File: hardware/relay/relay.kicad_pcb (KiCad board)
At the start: 2 copper layers, 65.5 x 22 mm, 18 parts, among them J1 GS3, J2 GS3, J3 CONN_02X04, J4 CONN_01X04, Q1 BC817-40, Q2 BC817-40, U1 ATTINY85-20SU, U2 ATTINY85-20PU

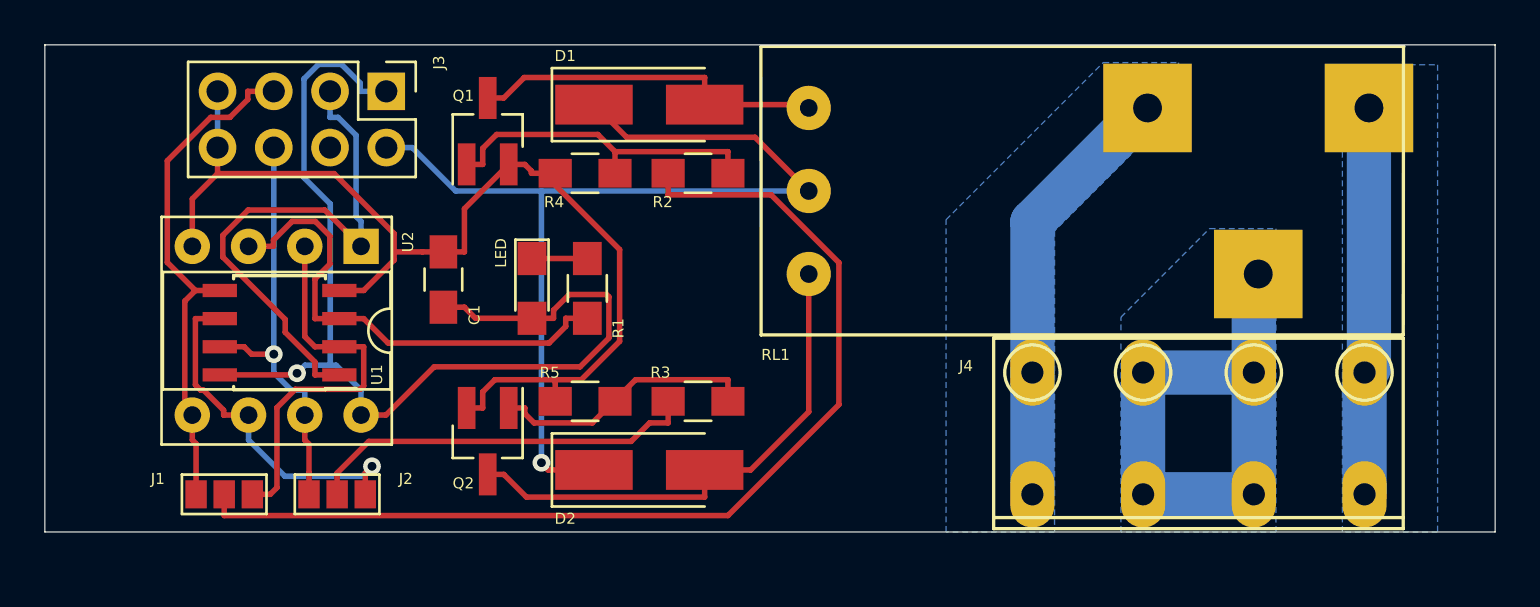
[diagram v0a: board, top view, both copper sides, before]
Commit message: Fix relay footprint
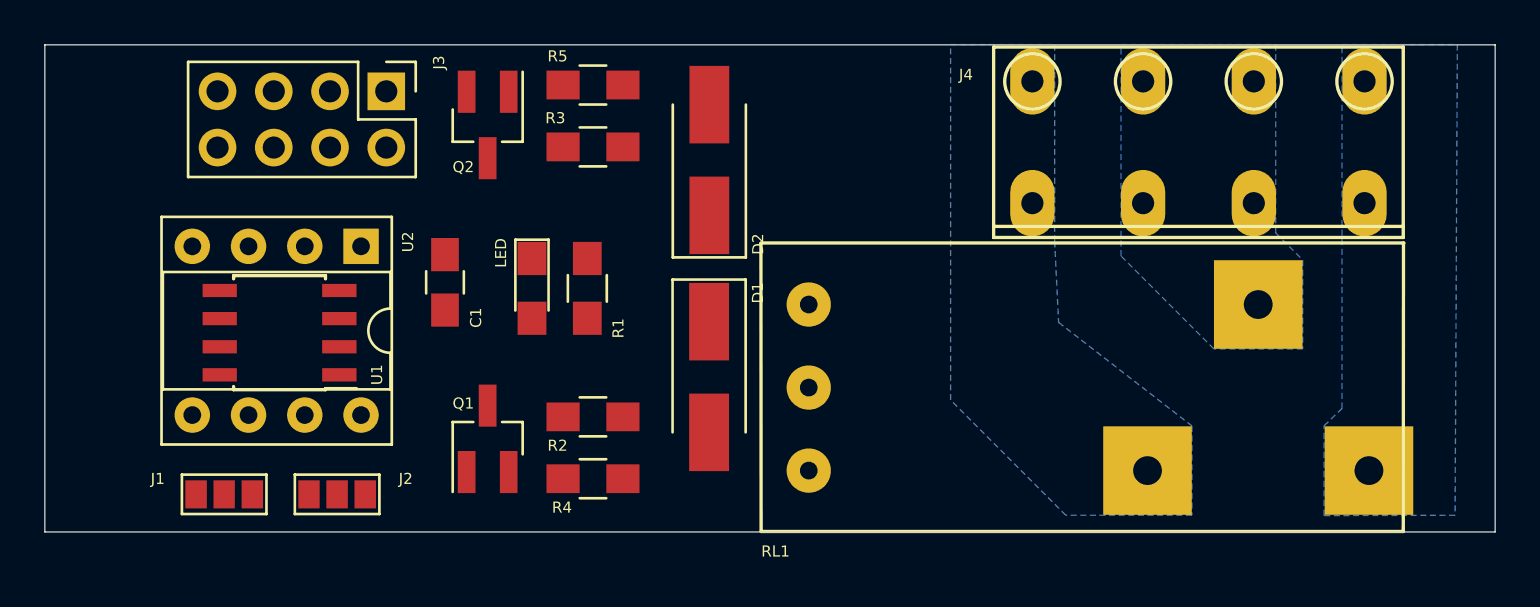
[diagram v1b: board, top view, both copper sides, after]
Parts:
- moved R5 14.3 mm to (74.8, 51.8)
- moved Q2 14.3 mm to (70.0, 53.6)
- moved D2 14.3 mm to (80.0, 55.2), turned to 90 degrees
- moved Q1 13.9 mm to (70.0, 67.8)
- moved R4 13.8 mm to (74.8, 69.6)
- moved J4 13.1 mm to (109.6, 57.1)
- moved D1 12.6 mm to (80.0, 65.0), turned to 270 degrees
- moved R3 12.4 mm to (74.8, 54.6)
- moved R2 12.0 mm to (74.8, 66.8)
- moved RL1 8.88 mm to (84.5, 65.5)
- moved C1 0.15 mm to (68.1, 60.7)
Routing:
- net GND: track 49.7 -> 0.00 mm
- net +3V3: track 49.2 -> 0.00 mm, vias 1 -> 0
- net Net-(J1-Pad2): track 47.2 -> 0.00 mm
- net +12V: track 46.0 -> 0.00 mm, vias 1 -> 0
- net /R_COM: track 25.8 -> 0.00 mm
- net /#RESET: track 24.3 -> 0.00 mm
- net /R_L2: track 23.5 -> 0.00 mm
- net /L1/SDA: track 23.4 -> 0.00 mm
- net /LED_PWM: track 22.0 -> 0.00 mm
- net /R_NC: track 19.6 -> 0.00 mm
- net /L2/SCL: track 19.3 -> 0.00 mm, vias 1 -> 0
- net /L1: track 17.9 -> 0.00 mm
- net Net-(J2-Pad2): track 17.8 -> 0.00 mm
- net /R_NO: track 17.5 -> 0.00 mm
- net /R_L1: track 16.2 -> 0.00 mm
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
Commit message: Fix relay footprint, swap relay and 240V terminals, rearange logic components for easier part placement.
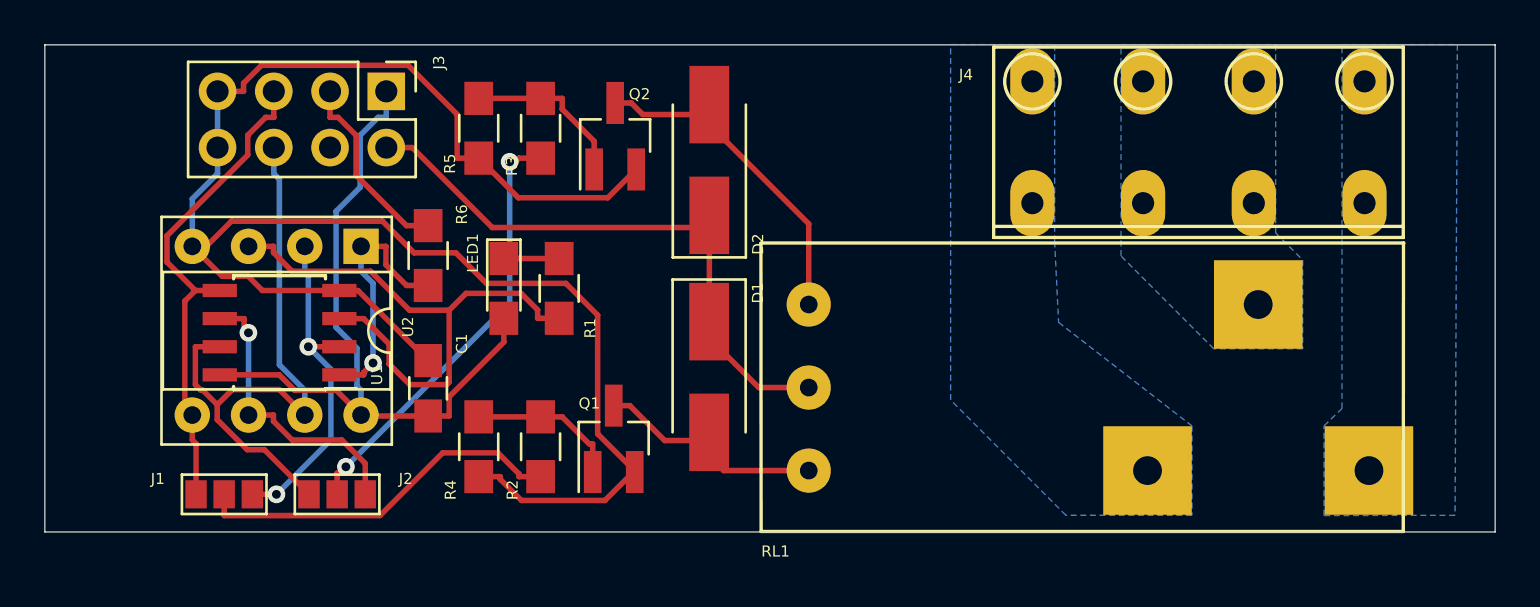
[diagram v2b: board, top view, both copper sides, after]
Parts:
- added R6: 10k, Resistors_SMD:R_0805_HandSoldering, F.Cu at (67.3, 59.5)
- moved Q2 5.78 mm to (75.8, 54.1), turned to 90 degrees
- moved Q1 5.69 mm to (75.7, 67.8)
- moved R5 5.52 mm to (69.6, 53.8), turned to 270 degrees
- moved R4 5.36 mm to (69.6, 68.2), turned to 270 degrees
- moved C1 4.85 mm to (67.3, 65.5)
- moved R2 2.72 mm to (72.4, 68.2), turned to 270 degrees
- moved R3 2.51 mm to (72.4, 53.8), turned to 270 degrees
- moved LED1 1.27 mm to (70.7, 61.0)
- moved R1 1.27 mm to (73.2, 61.0)
- renumbered LED to LED1
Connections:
- net /L1 renamed L1
- net /L1/SDA renamed L1_SDA
- net /L2 renamed L2
- net /L2/SCL renamed L2_SCL
- net /LED_PWM renamed LED_PWM
- net /R_COM renamed R_COM
- net /R_L1 renamed R_L1
- net /R_L2 renamed R_L2
- net /R_NC renamed R_NC
- net /R_NO renamed R_NO
- J3 pad 3: /#RESET -> Net-(J3-Pad3)
- U1 pad 1: /#RESET -> #RESET
- U2 pad 1: /#RESET -> #RESET
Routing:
- net GND: track 0.00 -> 80.4 mm
- net +3V3: track 0.00 -> 32.8 mm
- net L2_SCL: track 0.00 -> 27.8 mm
- net +12V: track 0.00 -> 27.1 mm
- net LED_PWM: track 0.00 -> 26.4 mm
- net L1_SDA: track 0.00 -> 22.5 mm
- net Net-(J2-Pad2): track 0.00 -> 19.8 mm, vias 0 -> 2
- net Net-(J1-Pad2): track 0.00 -> 16.9 mm
- net R_L2: track 0.00 -> 15.4 mm
- net L1: track 0.00 -> 15.2 mm, vias 0 -> 2
- net L2: track 0.00 -> 13.3 mm, vias 0 -> 1
- net #RESET: track 0.00 -> 11.6 mm, vias 0 -> 1
- net R_L1: track 0.00 -> 10.8 mm
- net Net-(J3-Pad3): track 0.00 -> 8.69 mm
- net Net-(Q2-Pad1): track 0.00 -> 7.57 mm
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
